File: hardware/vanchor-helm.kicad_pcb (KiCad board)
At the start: 2 copper layers, 0 parts

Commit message: feat: board generation - placement DRC-clean (100x120, Pi stacks below, courtyard-verified)
Co-Authored-By: Claude Fable 5 <noreply@anthropic.com>
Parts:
- added C1: 470u/63V, CP_Radial_D12.5mm_P5.00mm, F.Cu at (50.5, 116.0)
- added C10: 100n, C_Disc_D5.0mm_W2.5mm_P5.00mm, F.Cu at (106.5, 106.5)
- added C11: 100u, CP_Radial_D5.0mm_P2.00mm, F.Cu at (116.7, 105.0)
- added C12: 100n, C_Disc_D5.0mm_W2.5mm_P5.00mm, F.Cu at (74.5, 103.5)
- added C13: 100n, C_Disc_D5.0mm_W2.5mm_P5.00mm, F.Cu at (78.0, 103.5)
- added C2: 470u/63V, CP_Radial_D12.5mm_P5.00mm, F.Cu at (63.5, 116.0)
- added C3: 100u, CP_Radial_D6.3mm_P2.50mm, F.Cu at (76.0, 117.2)
- added C4: 100u/25V, CP_Radial_D6.3mm_P2.50mm, F.Cu at (83.0, 117.2)
- added C5: 100n, C_Disc_D5.0mm_W2.5mm_P5.00mm, F.Cu at (114.0, 82.5)
- added C6: 100n, C_Disc_D5.0mm_W2.5mm_P5.00mm, F.Cu at (65.5, 90.0)
- added C7: 100n, C_Disc_D5.0mm_W2.5mm_P5.00mm, F.Cu at (79.5, 90.0)
- added C8: 10u, CP_Radial_D5.0mm_P2.00mm, F.Cu at (111.0, 105.0)
- added C9: 100n, C_Disc_D5.0mm_W2.5mm_P5.00mm, F.Cu at (92.5, 90.0)
- added D10: BAT54S, SOT-23, F.Cu at (106.0, 39.0)
- added D11: BAT54S, SOT-23, F.Cu at (110.5, 39.0)
- added D4: BZX85C12, D_DO-41_SOD81_P10.16mm_Horizontal, F.Cu at (36.9, 100.0)
- added D5: SMCJ58A, D_SMC, F.Cu at (42.0, 105.0)
- added D6: BAT54S, SOT-23, F.Cu at (114.0, 86.0)
- added D7: 1N4007, D_DO-41_SOD81_P10.16mm_Horizontal, F.Cu at (101.0, 108.6)
- added D8: BAT54S, SOT-23, F.Cu at (70.0, 100.0)
- added D9: BAT54S, SOT-23, F.Cu at (70.0, 104.0)
- added F1: 10A blade, Fuseholder_Blade_Mini_Keystone_3568, F.Cu at (40.3, 122.0)
- added F2: MF-R200 2A, Fuse_Bourns_MF-RG400, F.Cu at (103.5, 123.4)
- added H1: MountingHole_3.2mm_M3, MountingHole_3.2mm_M3, F.Cu at (25.0, 25.0)
- added H2: MountingHole_3.2mm_M3, MountingHole_3.2mm_M3, F.Cu at (115.0, 25.0)
- added H3: MountingHole_3.2mm_M3, MountingHole_3.2mm_M3, F.Cu at (25.0, 135.0)
- added H4: MountingHole_3.2mm_M3, MountingHole_3.2mm_M3, F.Cu at (115.0, 135.0)
- added H5: MountingHole_2.7mm_M2.5, MountingHole_2.7mm_M2.5, F.Cu at (56.5, 45.5)
- added H6: MountingHole_2.7mm_M2.5, MountingHole_2.7mm_M2.5, F.Cu at (114.5, 45.5)
- added H7: MountingHole_2.7mm_M2.5, MountingHole_2.7mm_M2.5, F.Cu at (56.5, 94.5)
- added H8: MountingHole_2.7mm_M2.5, MountingHole_2.7mm_M2.5, F.Cu at (114.5, 94.5)
- added J1: PI_40PIN_STACK, PinSocket_2x20_P2.54mm_Vertical, B.Cu at (61.4, 46.8)
- added J10: DISP PWR 5V, JST_XH_B2B-XH-A_1x02_P2.50mm_Vertical, F.Cu at (115.5, 57.2)
- added J11: AS5600, JST_XH_B4B-XH-A_1x04_P2.50mm_Vertical, F.Cu at (115.5, 39.2)
- added J12: PICO UTIL, PinHeader_1x08_P2.54mm_Vertical, F.Cu at (29.1, 128.0)
- added J13: KNOB (VH/W/VL), TerminalBlock_CUI_TB007-508-03_1x03_P5.08mm_Horizontal, F.Cu at (89.6, 115.8)
- added J14: CONTACTOR 12V, TerminalBlock_CUI_TB007-508-02_1x02_P5.08mm_Horizontal, F.Cu at (83.2, 128.8)
- added J15: IBT-2, PinHeader_1x08_P2.54mm_Vertical, F.Cu at (55.1, 128.0)
- added J16: BATT_12-48V, TerminalBlock_CUI_TB007-508-02_1x02_P5.08mm_Horizontal, F.Cu at (27.2, 115.8)
- added J17: 12V_LINK, TerminalBlock_CUI_TB007-508-02_1x02_P5.08mm_Horizontal, F.Cu at (107.2, 115.8)
- added J2: PI_BREAKOUT, PinHeader_2x20_P2.54mm_Vertical, F.Cu at (23.2, 43.9)
- added J3: UART0 ttyAMA0, JST_XH_B4B-XH-A_1x04_P2.50mm_Vertical, F.Cu at (32.2, 26.5)
- added J4: UART2 ttyAMA2, JST_XH_B4B-XH-A_1x04_P2.50mm_Vertical, F.Cu at (45.8, 26.5)
- added J5: UART3 ttyAMA3, JST_XH_B4B-XH-A_1x04_P2.50mm_Vertical, F.Cu at (59.2, 26.5)
- added J6: UART4 ttyAMA4, JST_XH_B4B-XH-A_1x04_P2.50mm_Vertical, F.Cu at (72.8, 26.5)
- added J7: UART5 ttyAMA5, JST_XH_B4B-XH-A_1x04_P2.50mm_Vertical, F.Cu at (86.2, 26.5)
- added J8: I2C1 spare, JST_XH_B4B-XH-A_1x04_P2.50mm_Vertical, F.Cu at (99.8, 26.5)
- added J9: FAN 5V, PinHeader_1x02_P2.54mm_Vertical, F.Cu at (116.0, 124.7)
- added JP1: WIPER_SRC, SolderJumper-3_P1.3mm_Open_RoundedPad1.0x1.5mm, F.Cu at (108.0, 99.0)
- added LED1: green, LED_D5.0mm, F.Cu at (40.7, 35.0)
- added LED2: green, LED_D5.0mm, F.Cu at (53.7, 35.0)
- added LED3: green, LED_D5.0mm, F.Cu at (66.7, 35.0)
- added LED4: green, LED_D5.0mm, F.Cu at (79.7, 35.0)
- added LED5: yellow, LED_D5.0mm, F.Cu at (92.7, 35.0)
- added Q1: IRF9540N, TO-220-3_Vertical, F.Cu at (25.5, 101.0)
- added Q2: IRLZ44N, TO-220-3_Vertical, F.Cu at (83.5, 101.0)
- added R1: 47k, R_Axial_DIN0207_L6.3mm_D2.5mm_P10.16mm_Horizontal, F.Cu at (22.9, 105.5)
- added R10: 4.7k, R_Axial_DIN0207_L6.3mm_D2.5mm_P10.16mm_Horizontal, F.Cu at (88.9, 94.0)
- added R11: 100k, R_Axial_DIN0207_L6.3mm_D2.5mm_P10.16mm_Horizontal, F.Cu at (114.0, 75.1)
- added R12: 6.8k, R_Axial_DIN0207_L6.3mm_D2.5mm_P10.16mm_Horizontal, F.Cu at (118.0, 75.1)
- added R13: 1k, R_Axial_DIN0207_L6.3mm_D2.5mm_P10.16mm_Horizontal, F.Cu at (90.9, 40.5)
- added R14: 10k, R_Axial_DIN0207_L6.3mm_D2.5mm_P10.16mm_Horizontal, F.Cu at (104.0, 87.1)
- added R15: 1k, R_Axial_DIN0207_L6.3mm_D2.5mm_P10.16mm_Horizontal, F.Cu at (108.0, 87.1)
- added R16: 100R, R_Axial_DIN0207_L6.3mm_D2.5mm_P10.16mm_Horizontal, F.Cu at (80.9, 106.5)
- added R17: 100k, R_Axial_DIN0207_L6.3mm_D2.5mm_P10.16mm_Horizontal, F.Cu at (94.0, 109.1)
- added R18: 10k, R_Axial_DIN0207_L6.3mm_D2.5mm_P10.16mm_Horizontal, F.Cu at (55.9, 100.0)
- added R19: 10k, R_Axial_DIN0207_L6.3mm_D2.5mm_P10.16mm_Horizontal, F.Cu at (55.9, 104.0)
- added R2: 15k/0.5W, R_Axial_DIN0207_L6.3mm_D2.5mm_P10.16mm_Horizontal, F.Cu at (38.9, 40.5)
- added R20: 100R, R_Axial_DIN0207_L6.3mm_D2.5mm_P10.16mm_Horizontal, F.Cu at (100.9, 32.0)
- added R21: 100R, R_Axial_DIN0207_L6.3mm_D2.5mm_P10.16mm_Horizontal, F.Cu at (100.9, 35.5)
- added R3: 1k, R_Axial_DIN0207_L6.3mm_D2.5mm_P10.16mm_Horizontal, F.Cu at (51.9, 40.5)
- added R4: 4.7k, R_Axial_DIN0207_L6.3mm_D2.5mm_P10.16mm_Horizontal, F.Cu at (64.9, 40.5)
- added R5: 2.2k, R_Axial_DIN0207_L6.3mm_D2.5mm_P10.16mm_Horizontal, F.Cu at (25.9, 39.0)
- added R6: 2.2k, R_Axial_DIN0207_L6.3mm_D2.5mm_P10.16mm_Horizontal, F.Cu at (25.9, 35.0)
- added R7: 1k, R_Axial_DIN0207_L6.3mm_D2.5mm_P10.16mm_Horizontal, F.Cu at (77.9, 40.5)
- added R8: 1k, R_Axial_DIN0207_L6.3mm_D2.5mm_P10.16mm_Horizontal, F.Cu at (60.9, 94.0)
- added R9: 4.7k, R_Axial_DIN0207_L6.3mm_D2.5mm_P10.16mm_Horizontal, F.Cu at (74.9, 94.0)
- added U1: Pico 2, RaspberryPi_Pico_TH_SWD, F.Cu at (109.0, 53.0)
- added U2: 74AHCT125, DIP-14_W7.62mm_Socket, F.Cu at (75.6, 78.2)
- added U3: X9C103, DIP-8_W7.62mm_Socket, F.Cu at (86.8, 78.2)
- added U4: MCP6002-I/P, DIP-8_W7.62mm_Socket, F.Cu at (98.8, 78.2)
- added U5: D36V50F5, Pololu_D36V50Fx, F.Cu at (40.5, 55.0)
- added U6: D36V50F12, Pololu_D36V50Fx, F.Cu at (40.5, 83.0)
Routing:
- added copper zone on B.Cu, net GND
- added copper zone on F.Cu, net GND
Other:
- board outline added: 100 x 120 mm

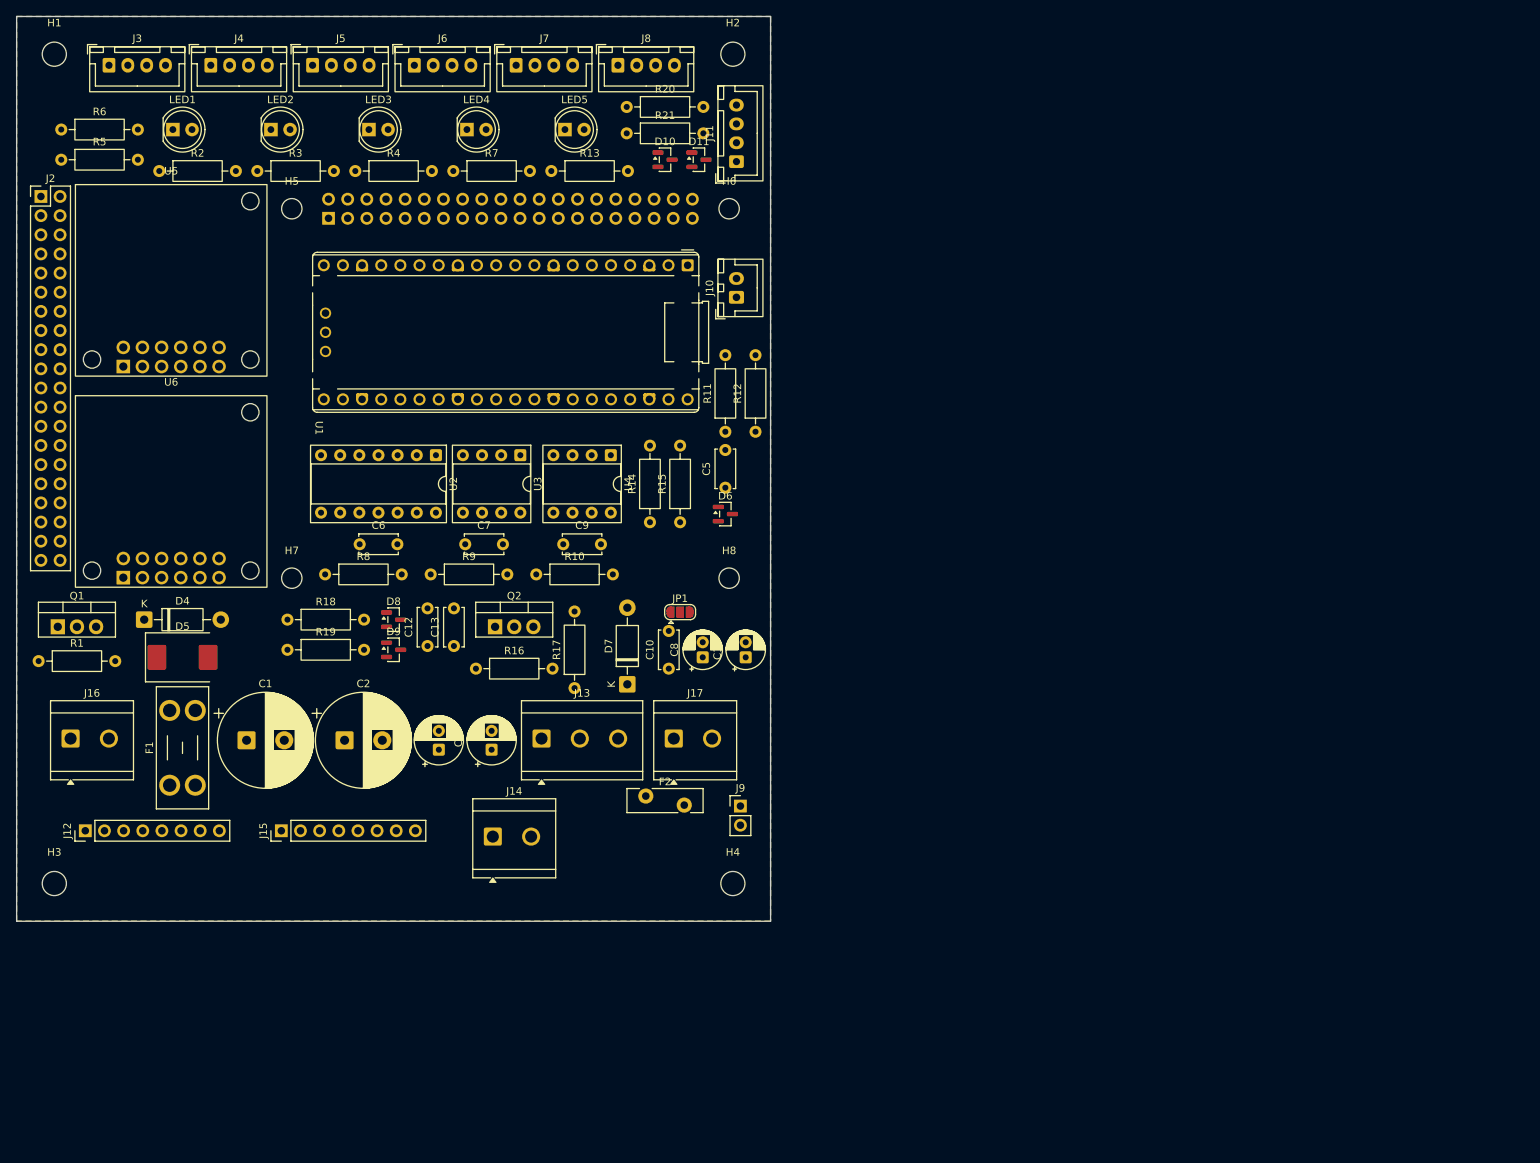
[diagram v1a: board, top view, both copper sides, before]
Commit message: feat: on-board 800W H-bridge (HIP4082 + 8 FET, ACS758, M5 lugs) + BTN8982 servo bridge; 160x120 board, placement DRC-clean
Co-Authored-By: Claude Fable 5 <noreply@anthropic.com>
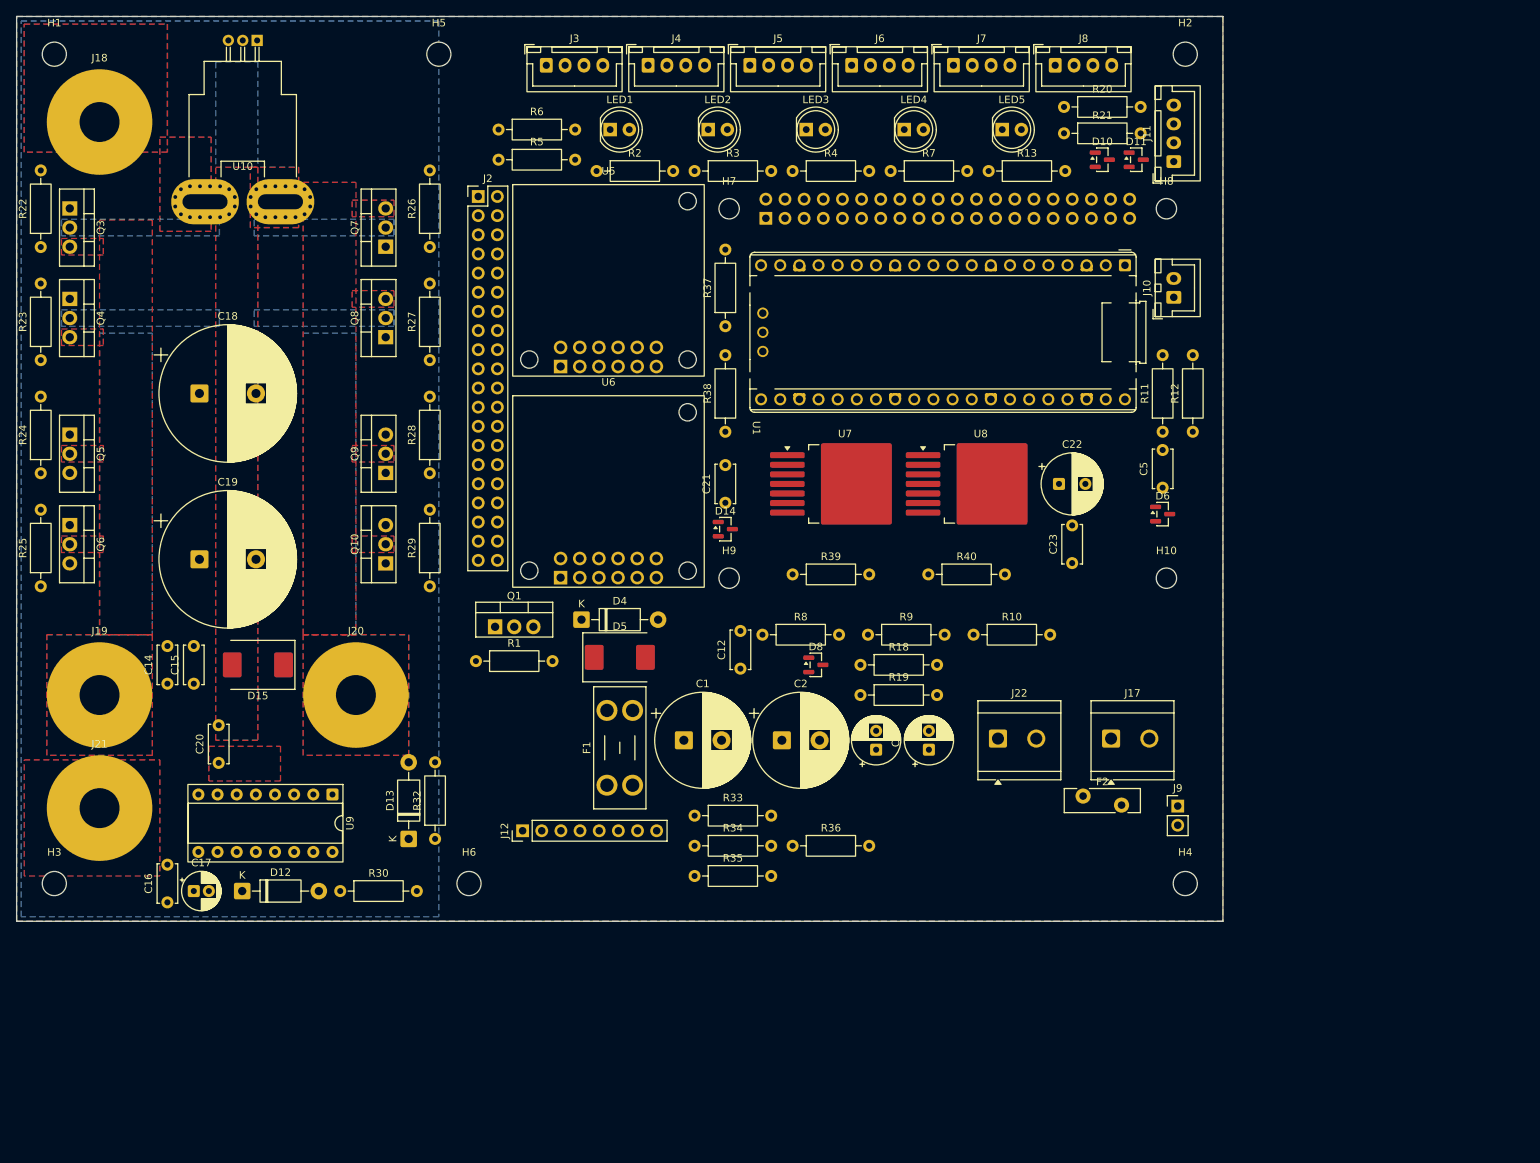
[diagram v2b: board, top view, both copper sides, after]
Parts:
- removed C10, C13, C6, C7, C9: 100n, C_Disc_D5.0mm_W2.5mm_P5.00mm
- removed C11: 100u, CP_Radial_D5.0mm_P2.00mm
- removed C8: 10u, CP_Radial_D5.0mm_P2.00mm
- removed D7: 1N4007, D_DO-41_SOD81_P10.16mm_Horizontal
- removed D9: BAT54S, SOT-23
- removed J13: KNOB (VH/W/VL), TerminalBlock_CUI_TB007-508-03_1x03_P5.08mm_Horizontal
- removed J14: CONTACTOR 12V, TerminalBlock_CUI_TB007-508-02_1x02_P5.08mm_Horizontal
- removed J15: IBT-2, PinHeader_1x08_P2.54mm_Vertical
- removed J16: BATT_12-48V, TerminalBlock_CUI_TB007-508-02_1x02_P5.08mm_Horizontal
- removed JP1: WIPER_SRC, SolderJumper-3_P1.3mm_Open_RoundedPad1.0x1.5mm
- removed Q2: IRLZ44N, TO-220-3_Vertical
- removed R14: 10k, R_Axial_DIN0207_L6.3mm_D2.5mm_P10.16mm_Horizontal
- removed R15: 1k, R_Axial_DIN0207_L6.3mm_D2.5mm_P10.16mm_Horizontal
- removed R16: 100R, R_Axial_DIN0207_L6.3mm_D2.5mm_P10.16mm_Horizontal
- removed R17: 100k, R_Axial_DIN0207_L6.3mm_D2.5mm_P10.16mm_Horizontal
- removed U2: 74AHCT125, DIP-14_W7.62mm_Socket
- removed U3: X9C103, DIP-8_W7.62mm_Socket
- removed U4: MCP6002-I/P, DIP-8_W7.62mm_Socket
- added C14: 1u/50V, C_Disc_D5.0mm_W2.5mm_P5.00mm, F.Cu at (40.0, 108.5)
- added C15: 1u/50V, C_Disc_D5.0mm_W2.5mm_P5.00mm, F.Cu at (43.5, 108.5)
- added C16: 100n, C_Disc_D5.0mm_W2.5mm_P5.00mm, F.Cu at (40.0, 137.5)
- added C17: 10u/25V, CP_Radial_D5.0mm_P2.00mm, F.Cu at (43.5, 136.0)
- added C18: 2200u/63V, CP_Radial_D18.0mm_P7.50mm, F.Cu at (44.2, 70.0)
- added C19: 2200u/63V, CP_Radial_D18.0mm_P7.50mm, F.Cu at (44.2, 92.0)
- added C20: 1u/100V film, C_Disc_D5.0mm_W2.5mm_P5.00mm, F.Cu at (46.8, 119.0)
- added C21: 100n, C_Disc_D5.0mm_W2.5mm_P5.00mm, F.Cu at (114.0, 84.5)
- added C22: 220u/25V, CP_Radial_D8.0mm_P3.50mm, F.Cu at (158.3, 82.0)
- added C23: 100n, C_Disc_D5.0mm_W2.5mm_P5.00mm, F.Cu at (160.0, 92.5)
- added D12: UF4007, D_DO-41_SOD81_P10.16mm_Horizontal, F.Cu at (49.9, 136.0)
- added D13: UF4007, D_DO-41_SOD81_P10.16mm_Horizontal, F.Cu at (72.0, 129.1)
- added D14: BAT54S, SOT-23, F.Cu at (114.0, 88.0)
- added D15: SMCJ58A, D_SMC, F.Cu at (52.0, 106.0)
- added H10: MountingHole_2.7mm_M2.5, MountingHole_2.7mm_M2.5, F.Cu at (172.5, 94.5)
- added H9: MountingHole_2.7mm_M2.5, MountingHole_2.7mm_M2.5, F.Cu at (114.5, 94.5)
- added J18: LUG BATT+, Lug_M5, F.Cu at (31.0, 34.0)
- added J19: LUG MOTOR A, Lug_M5, F.Cu at (31.0, 110.0)
- added J20: LUG MOTOR B, Lug_M5, F.Cu at (65.0, 110.0)
- added J21: LUG GND, Lug_M5, F.Cu at (31.0, 125.0)
- added J22: SERVO MOTOR, TerminalBlock_CUI_TB007-508-02_1x02_P5.08mm_Horizontal, F.Cu at (150.2, 115.8)
- added Q10: IRF100P219, TO-220-3_Vertical, F.Cu at (69.0, 92.5)
- added Q3: IRF100P219, TO-220-3_Vertical, F.Cu at (27.1, 45.5)
- added Q4: IRF100P219, TO-220-3_Vertical, F.Cu at (27.1, 57.5)
- added Q5: IRF100P219, TO-220-3_Vertical, F.Cu at (27.1, 75.5)
- added Q6: IRF100P219, TO-220-3_Vertical, F.Cu at (27.1, 87.5)
- added Q7: IRF100P219, TO-220-3_Vertical, F.Cu at (69.0, 50.5)
- added Q8: IRF100P219, TO-220-3_Vertical, F.Cu at (69.0, 62.5)
- added Q9: IRF100P219, TO-220-3_Vertical, F.Cu at (69.0, 80.5)
- added R22: 10R, R_Axial_DIN0207_L6.3mm_D2.5mm_P10.16mm_Horizontal, F.Cu at (23.2, 50.6)
- added R23: 10R, R_Axial_DIN0207_L6.3mm_D2.5mm_P10.16mm_Horizontal, F.Cu at (23.2, 65.6)
- added R24: 10R, R_Axial_DIN0207_L6.3mm_D2.5mm_P10.16mm_Horizontal, F.Cu at (23.2, 80.6)
- added R25: 10R, R_Axial_DIN0207_L6.3mm_D2.5mm_P10.16mm_Horizontal, F.Cu at (23.2, 95.6)
- added R26: 10R, R_Axial_DIN0207_L6.3mm_D2.5mm_P10.16mm_Horizontal, F.Cu at (74.8, 50.6)
- added R27: 10R, R_Axial_DIN0207_L6.3mm_D2.5mm_P10.16mm_Horizontal, F.Cu at (74.8, 65.6)
- added R28: 10R, R_Axial_DIN0207_L6.3mm_D2.5mm_P10.16mm_Horizontal, F.Cu at (74.8, 80.6)
- added R29: 10R, R_Axial_DIN0207_L6.3mm_D2.5mm_P10.16mm_Horizontal, F.Cu at (74.8, 95.6)
- added R30: 150k, R_Axial_DIN0207_L6.3mm_D2.5mm_P10.16mm_Horizontal, F.Cu at (62.9, 136.0)
- added R32: 10k, R_Axial_DIN0207_L6.3mm_D2.5mm_P10.16mm_Horizontal, F.Cu at (75.5, 129.1)
- added R33: 100k, R_Axial_DIN0207_L6.3mm_D2.5mm_P10.16mm_Horizontal, F.Cu at (109.9, 126.0)
- added R34: 100k, R_Axial_DIN0207_L6.3mm_D2.5mm_P10.16mm_Horizontal, F.Cu at (109.9, 130.0)
- added R35: 100k, R_Axial_DIN0207_L6.3mm_D2.5mm_P10.16mm_Horizontal, F.Cu at (109.9, 134.0)
- added R36: 100k, R_Axial_DIN0207_L6.3mm_D2.5mm_P10.16mm_Horizontal, F.Cu at (122.9, 130.0)
- added R37: 10k, R_Axial_DIN0207_L6.3mm_D2.5mm_P10.16mm_Horizontal, F.Cu at (114.0, 61.1)
- added R38: 20k, R_Axial_DIN0207_L6.3mm_D2.5mm_P10.16mm_Horizontal, F.Cu at (114.0, 75.1)
- added R39: 51k, R_Axial_DIN0207_L6.3mm_D2.5mm_P10.16mm_Horizontal, F.Cu at (122.9, 94.0)
- added R40: 51k, R_Axial_DIN0207_L6.3mm_D2.5mm_P10.16mm_Horizontal, F.Cu at (140.9, 94.0)
- added U10: ACS758LCB-100B, Allegro_CB_PFF, F.Cu at (51.9, 23.2)
- added U7: BTN8982TA, TO-263-7_TabPin4, F.Cu at (129.9, 82.0)
- added U8: BTN8982TA, TO-263-7_TabPin4, F.Cu at (147.9, 82.0)
- added U9: HIP4082IPZ, DIP-16_W7.62mm_Socket, F.Cu at (61.9, 123.2)
- H5, H6: value MountingHole_2.7mm_M2.5 -> MountingHole_3.2mm_M3; footprint MountingHole_2.7mm_M2.5 -> MountingHole_3.2mm_M3
- R19: value 10k -> 1k
- moved H6 95.9 mm to (80.0, 135.0)
- moved R18 76.2 mm to (131.9, 106.0)
- moved R19 76.2 mm to (131.9, 110.0)
- moved H7 75.9 mm to (114.5, 45.5)
- moved H8 75.9 mm to (172.5, 45.5)
- moved H2 60.0 mm to (175.0, 25.0)
- moved H4 60.0 mm to (175.0, 135.0)
- moved R8 58.5 mm to (118.9, 102.0)
- moved R10 58.5 mm to (146.9, 102.0)
- moved R9 58.5 mm to (132.9, 102.0)
- moved C1 58.0 mm to (108.5, 116.0)
- moved C2 58.0 mm to (121.5, 116.0)
- moved J1 58.0 mm to (119.4, 46.8)
- moved C5 58.0 mm to (172.0, 82.5)
- moved D10 58.0 mm to (164.0, 39.0)
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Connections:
- net ISENSE_R renamed SERVO_IS
- F1 pad 1: /power/BATT_IN -> VBAT_PWR
- R18 pad 1: /servo/RIS_RAW -> /servo/SERVO_IS_RAW
- R19 pad 1: /servo/LIS_RAW -> /servo/SERVO_IS_RAW
- R19 pad 2: ISENSE_L -> GND
- U1 pad 16: DP_INC_3 -> THR_AHI
- U1 pad 17: DP_UD_3 -> THR_BHI
- U1 pad 19: DP_CS_3 -> THR_ALI
- U1 pad 20: THR_PWM_3 -> THR_BLI
- U1 pad 21: CONT_GATE_3 -> THR_DIS
- U1 pad 32: ISENSE_L -> THR_IS
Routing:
- added copper zone on B.Cu, net MOTOR_A
- added copper zone on F.Cu, net MOTOR_A
- added copper zone on B.Cu, net MOTOR_B
- added copper zone on F.Cu, net MOTOR_B
- added copper zone on B.Cu, net VBAT_PWR
- added copper zone on F.Cu, net VBAT_PWR
- added copper zone on B.Cu, net VBRIDGE
- added copper zone on F.Cu, net VBRIDGE
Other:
- board size 100 x 120 mm -> 160 x 120 mm
